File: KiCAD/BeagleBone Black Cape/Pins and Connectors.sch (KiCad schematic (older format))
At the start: 12 parts, among them J9 01x06_Stackable Header, P8 02x23_Stackable Header, P9 02x23_Stackable Header, SW1 W5500_RST, SW2 SYS_RST, SW3 Power

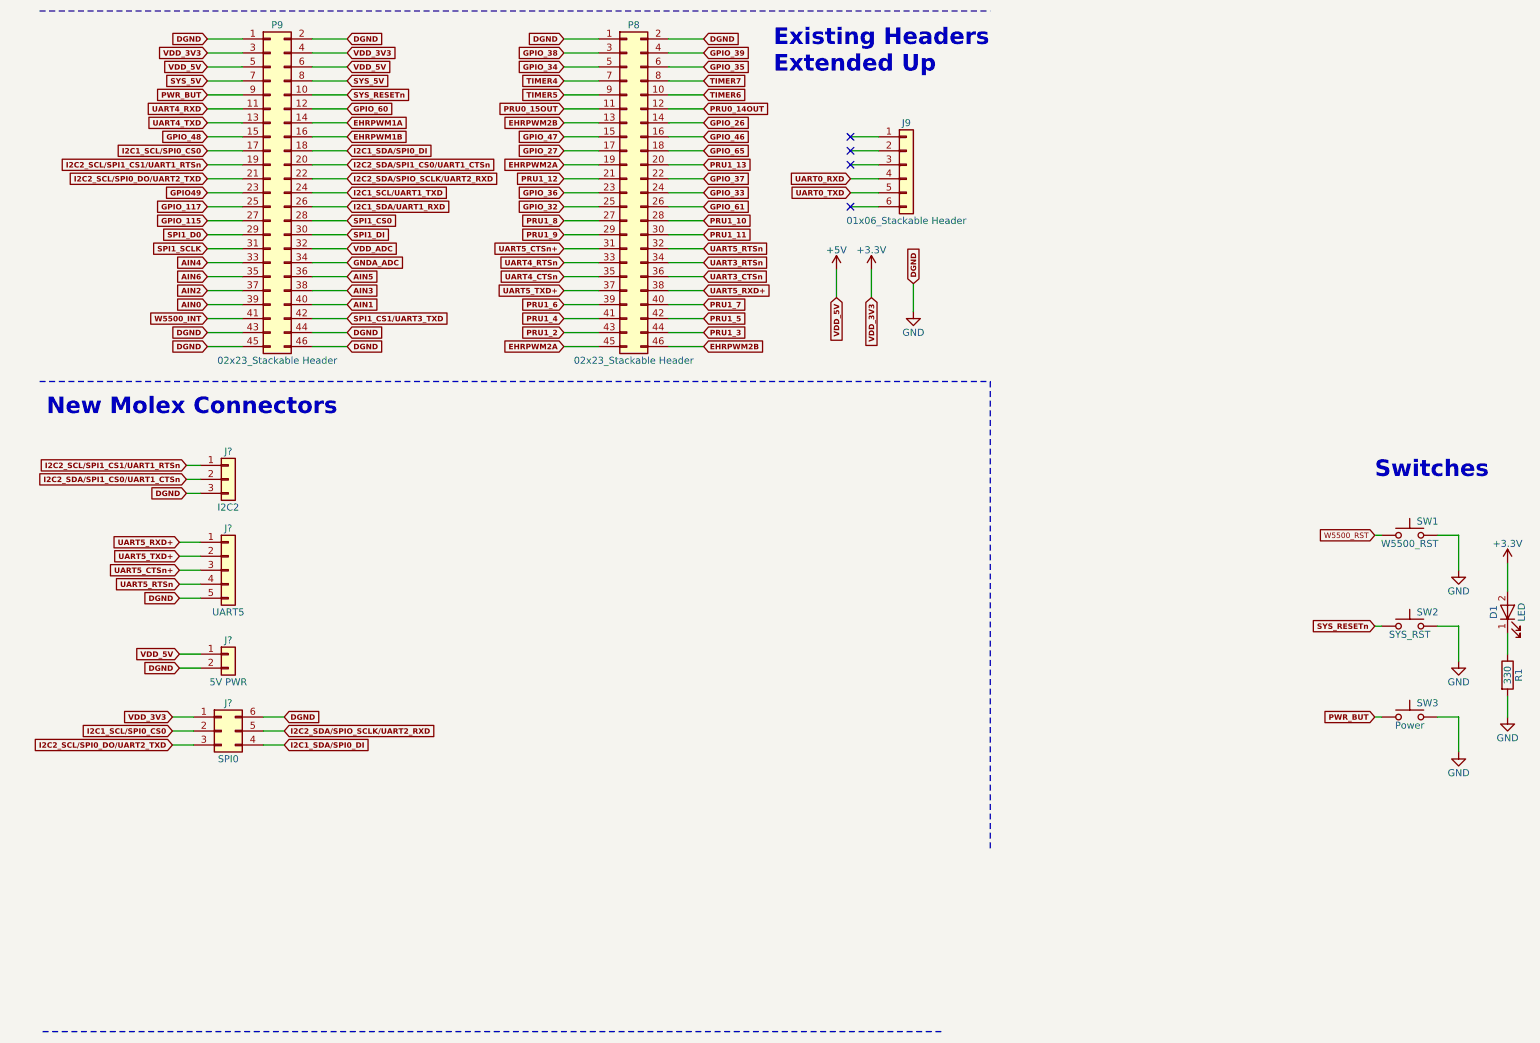
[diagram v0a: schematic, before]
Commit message: BeagleBone Updated, headers need to be moved into proper spot
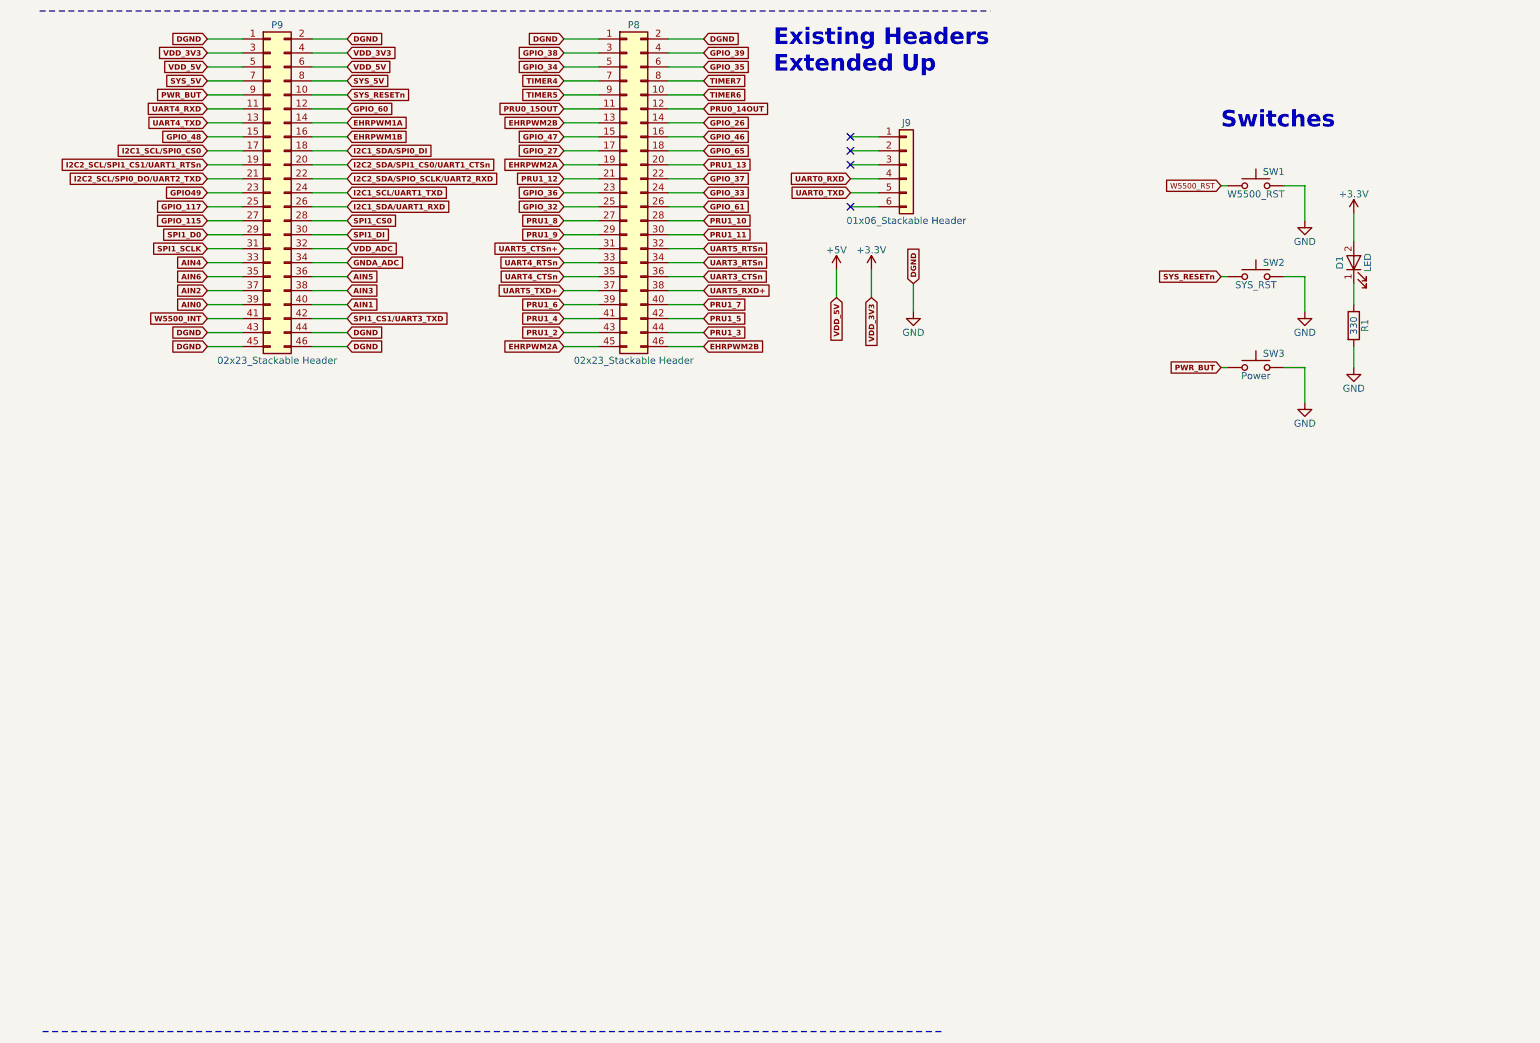
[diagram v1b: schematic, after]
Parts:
- removed J?: I2C2, symbol Conn_01x03
- removed J?: 5V PWR, symbol Conn_01x02
- removed J?: SPI0, symbol Conn_02x03_Counter_Clockwise
- removed J?: UART5, symbol Conn_01x05
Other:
- note removed: "New Molex Connectors"
- moved on the sheet: D1, R1, SW1, SW2, SW3
